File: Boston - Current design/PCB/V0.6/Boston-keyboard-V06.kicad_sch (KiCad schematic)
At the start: 601 parts, among them J701 Conn_01x02_Female, J702 Conn_01x03_Female, J705 TYPE-C-31-M12_13, J706 Conn_ARM_JTAG_SWD_10, Q701 DTC123J, Q702 AO4406AL, SW1 MXSwitch, SW10 MXSwitch, SW100 MXSwitch, SW101 MXSwitch, SW102 MXSwitch, SW103 MXSwitch, SW104 MXSwitch, SW105-1 MXSwitch, SW105-2 MXSwitch, SW106 MXSwitch, SW107 MXSwitch, SW108 MXSwitch, SW109 MXSwitch, SW11 MXSwitch, SW110 MXSwitch, SW111 MXSwitch, SW112 MXSwitch, SW113 MXSwitch, SW114 MXSwitch, SW115 MXSwitch, SW116 MXSwitch, SW117 MXSwitch, SW118 MXSwitch, SW119 MXSwitch, SW12 MXSwitch, SW120 MXSwitch, SW121 MXSwitch, SW122 MXSwitch, SW123 MXSwitch, SW124-1 MXSwitch, SW124-2 MXSwitch, SW125 MXSwitch, SW126 Rotary_Encoder_Switch_Chassis, SW127 MXSwitch, SW128 MXSwitch, SW129 MXSwitch, SW13 MXSwitch, SW14 MXSwitch, SW15 MXSwitch, SW16 MXSwitch, SW17 MXSwitch, SW18 MXSwitch, SW19 MXSwitch, SW2 MXSwitch, SW20-1 MXSwitch, SW20-2 MXSwitch, SW200 SW_Push, SW21 MXSwitch, SW22 MXSwitch, SW23 MXSwitch, SW24 MXSwitch, SW25 MXSwitch, SW26 MXSwitch, SW27 MXSwitch, SW28 MXSwitch, SW29 MXSwitch, SW3 MXSwitch, SW30 MXSwitch, SW31 MXSwitch, SW32 MXSwitch, SW33 MXSwitch, SW34 MXSwitch, SW35 MXSwitch, SW36 MXSwitch, SW37 MXSwitch, SW38 MXSwitch, SW39-1 MXSwitch, SW39-2 MXSwitch, SW39-3 MXSwitch, SW4-1 MXSwitch, SW4-2 MXSwitch, SW40 MXSwitch, SW41 MXSwitch, SW42 MXSwitch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

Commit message: Added capacitors to reduce EMI from backlight
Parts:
- added C2, C720, C723, C726, C727, C730, C731, C734, C735, C737, C738, C741, C742, C745, C746: 100nF, Capacitor_SMD:C_0805_2012Metric_Pad1.15x1.40mm_HandSolder, symbol Device:C
- added C716: 100n, Capacitor_SMD:C_0805_2012Metric_Pad1.15x1.40mm_HandSolder, symbol Device:C
- added C717, C718: 22uF, Capacitor_SMD:C_1206_3216Metric_Pad1.42x1.75mm_HandSolder, symbol Device:C
- added C721, C722, C724, C725, C728, C729, C732, C733, C736, C739, C740, C743, C744: 10u, Capacitor_SMD:C_1206_3216Metric_Pad1.42x1.75mm_HandSolder, symbol Device:C
- C704, C713: value 10u -> 22uF
- C711: value 22uF -> 10u
- L701: value L -> 6.8uH; footprint Inductor_SMD:L_Taiyo-Yuden_NR-50xx_HandSoldering -> SumidaInductor:Sumida0624CDMCC
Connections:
- net +3V3: now also C704.1, C2.1, C717.1, C718.1, C720.1, C721.1, C722.1, C723.1, C724.1, C725.1, C726.1, C727.1, C728.1, C729.1, C730.1, C731.1, C732.1, C733.1, C734.1, C735.1, C736.1, C737.1, C738.1, C739.1, C740.1, C741.1, C742.1, C743.1, C744.1, C745.1, C746.1
- net +5V: now also C716.1; no longer C704.1
- net GND: now also C716.2, C717.2, C718.2, C720.2; no longer C711.2
- net LED_switch: now also C711.2, C2.2, C721.2, C722.2, C723.2, C724.2, C725.2, C726.2, C727.2, C728.2, C729.2, C730.2, C731.2, C732.2, C733.2, C734.2, C735.2, C736.2, C737.2, C738.2, C739.2, C740.2, C741.2, C742.2, C743.2, C744.2, C745.2, C746.2
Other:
- note added: "Sumida 0624CDMCCDS-6R8MC"

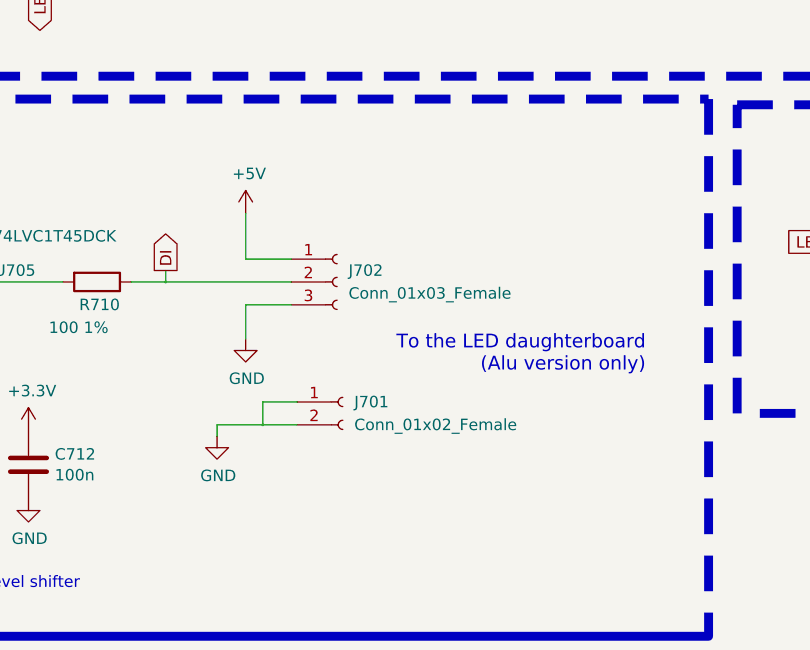
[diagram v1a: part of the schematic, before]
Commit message: More vias and tuning of ground planes for EMI purposes
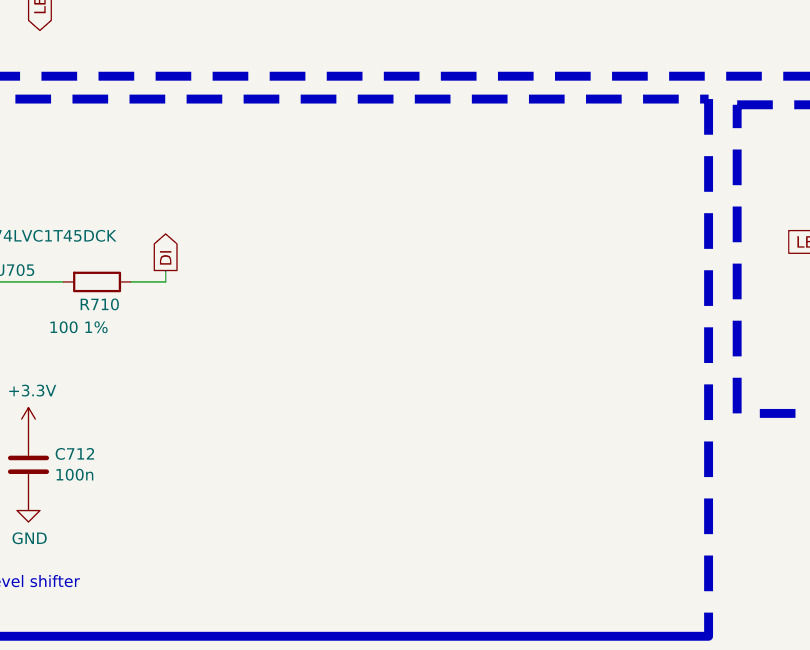
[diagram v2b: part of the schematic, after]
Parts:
- removed J701: Conn_01x02_Female, Connector_PinSocket_2.54mm:PinSocket_1x02_P2.54mm_Vertical, symbol Connector:Conn_01x02_Female
- removed J702: Conn_01x03_Female, Connector_PinSocket_2.54mm:PinSocket_1x03_P2.54mm_Vertical, symbol Connector:Conn_01x03_Female
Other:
- note removed: "To the LED daughterboard (Alu version only)"
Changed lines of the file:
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@@
   (junction (at 205.74 176.53) (diameter 0.3048) (color 0 0 0 0))
   (junction (at 205.74 204.47) (diameter 0.3048) (color 0 0 0 0))
-  (junction (at 205.74 469.265) (diameter 0.3048) (color 0 0 0 0))
   (junction (at 207.01 233.68) (diameter 0.3048) (color 0 0 0 0))
   (junction (at 208.28 234.95) (diameter 0.3048) (color 0 0 0 0))
@@
   (junction (at 213.36 408.94) (diameter 0.3048) (color 0 0 0 0))
   (junction (at 213.36 424.18) (diameter 0.3048) (color 0 0 0 0))
-  (junction (at 216.535 485.14) (diameter 0.3048) (color 0 0 0 0))
   (junction (at 217.17 35.56) (diameter 0.3048) (color 0 0 0 0))
   (junction (at 217.17 62.23) (diameter 0.3048) (color 0 0 0 0))
@@
     (stroke (width 0) (type solid) (color 0 0 0 0))
   )
-  (wire (pts (xy 205.74 469.265) (xy 219.71 469.265))
-    (stroke (width 0) (type solid) (color 0 0 0 0))
-  )
   (wire (pts (xy 207.01 233.68) (xy 205.74 233.68))
     (stroke (width 0) (type solid) (color 0 0 0 0))
@@
     (stroke (width 0) (type solid) (color 0 0 0 0))
   )
-  (wire (pts (xy 211.455 485.14) (xy 216.535 485.14))
-    (stroke (width 0) (type solid) (color 0 0 0 0))
-  )
-  (wire (pts (xy 211.455 486.41) (xy 211.455 485.14))
-    (stroke (width 0) (type solid) (color 0 0 0 0))
-  )
   (wire (pts (xy 213.36 283.21) (xy 204.47 283.21))
     (stroke (width 0) (type solid) (color 0 0 0 0))
@@
     (stroke (width 0) (type solid) (color 0 0 0 0))
   )
-  (wire (pts (xy 214.63 466.725) (xy 214.63 461.645))
-    (stroke (width 0) (type solid) (color 0 0 0 0))
-  )
-  (wire (pts (xy 214.63 471.805) (xy 214.63 475.615))
-    (stroke (width 0) (type solid) (color 0 0 0 0))
-  )
-  (wire (pts (xy 216.535 482.6) (xy 216.535 485.14))
-    (stroke (width 0) (type solid) (color 0 0 0 0))
-  )
-  (wire (pts (xy 216.535 485.14) (xy 220.345 485.14))
-    (stroke (width 0) (type solid) (color 0 0 0 0))
-  )
   (wire (pts (xy 217.17 35.56) (xy 182.88 35.56))
     (stroke (width 0) (type solid) (color 0 0 0 0))
@@
     (stroke (width 0) (type solid) (color 0 0 0 0))
   )
-  (wire (pts (xy 219.71 466.725) (xy 214.63 466.725))
-    (stroke (width 0) (type solid) (color 0 0 0 0))
-  )
-  (wire (pts (xy 219.71 471.805) (xy 214.63 471.805))
-    (stroke (width 0) (type solid) (color 0 0 0 0))
-  )
-  (wire (pts (xy 220.345 482.6) (xy 216.535 482.6))
-    (stroke (width 0) (type solid) (color 0 0 0 0))
-  )
   (wire (pts (xy 222.25 283.21) (xy 213.36 283.21))
     (stroke (width 0) (type solid) (color 0 0 0 0))
@@
     (effects (font (size 1.27 1.27)) (justify left bottom))
   )
-  (text "To the LED daughterboard\n(Alu version only)" (at 259.08 479.425 180)
-    (effects (font (size 1.524 1.524)) (justify right bottom))
-  )
   (text "RGB LED stuff" (at 266.7 514.985 180)
     (effects (font (size 3.175 3.175)) (justify right bottom))
@@
     (pin "1")
   )
-  (symbol (lib_id "power:+5V") (at 214.63 461.645 0) (unit 1)
-    (in_bom yes) (on_board yes)
-    (property "Reference" "#PWR0108" (id 0) (at 214.63 465.455 0)
-      (effects (font (size 1.27 1.27)) hide)
-    )
-    (property "Value" "+5V" (id 1) (at 215.011 457.2508 0))
-    (property "Footprint" "" (id 2) (at 214.63 461.645 0)
-      (effects (font (size 1.27 1.27)) hide)
-    )
-    (property "Datasheet" "" (id 3) (at 214.63 461.645 0)
-      (effects (font (size 1.27 1.27)) hide)
-    )
-    (pin "1")
-  )
   (symbol (lib_id "power:+3.3V") (at 315.595 389.255 0) (unit 1)
     (in_bom yes) (on_board yes)
@@
     (pin "1")
   )
-  (symbol (lib_id "power:GND") (at 211.455 486.41 0) (unit 1)
-    (in_bom yes) (on_board yes)
-    (property "Reference" "#PWR0701" (id 0) (at 211.455 492.76 0)
-      (effects (font (size 1.27 1.27)) hide)
-    )
-    (property "Value" "GND" (id 1) (at 211.582 490.8042 0))
-    (property "Footprint" "" (id 2) (at 211.455 486.41 0)
-      (effects (font (size 1.27 1.27)) hide)
-    )
-    (property "Datasheet" "" (id 3) (at 211.455 486.41 0)
-      (effects (font (size 1.27 1.27)) hide)
-    )
-    (pin "1")
-  )
-  (symbol (lib_id "power:GND") (at 214.63 475.615 0) (unit 1)
-    (in_bom yes) (on_board yes)
-    (property "Reference" "#PWR0109" (id 0) (at 214.63 481.965 0)
-      (effects (font (size 1.27 1.27)) hide)
-    )
-    (property "Value" "GND" (id 1) (at 214.757 480.0092 0))
-    (property "Footprint" "" (id 2) (at 214.63 475.615 0)
-      (effects (font (size 1.27 1.27)) hide)
-    )
-    (property "Datasheet" "" (id 3) (at 214.63 475.615 0)
-      (effects (font (size 1.27 1.27)) hide)
-    )
-    (pin "1")
-  )
   (symbol (lib_id "power:GND") (at 314.96 476.25 0) (unit 1)
     (in_bom yes) (on_board yes)
@@
     (pin "2")
   )
-  (symbol (lib_id "Connector:Conn_01x02_Female") (at 225.425 482.6 0) (unit 1)
-    (in_bom yes) (on_board yes)
-    (property "Reference" "J701" (id 0) (at 226.695 482.6 0)
-      (effects (font (size 1.27 1.27)) (justify left))
-    )
-    (property "Value" "Conn_01x02_Female" (id 1) (at 226.695 485.14 0)
-      (effects (font (size 1.27 1.27)) (justify left))
-    )
-    (property "Footprint" "Connector_PinSocket_2.54mm:PinSocket_1x02_P2.54mm_Vertical" (id 2) (at 225.425 482.6 0)
-      (effects (font (size 1.27 1.27)) hide)
-    )
-    (property "Datasheet" "~" (id 3) (at 225.425 482.6 0)
-      (effects (font (size 1.27 1.27)) hide)
-    )
-    (pin "1")
-    (pin "2")
-  )
   (symbol (lib_id "Device:LED") (at 19.05 337.82 90) (unit 1)
     (in_bom yes) (on_board yes)
@@
     (pin "2")
   )
-  (symbol (lib_id "Connector:Conn_01x03_Female") (at 224.79 469.265 0) (unit 1)
-    (in_bom yes) (on_board yes)
-    (property "Reference" "J702" (id 0) (at 226.06 467.995 0)
-      (effects (font (size 1.27 1.27)) (justify left))
-    )
-    (property "Value" "Conn_01x03_Female" (id 1) (at 226.06 470.535 0)
-      (effects (font (size 1.27 1.27)) (justify left))
-    )
-    (property "Footprint" "Connector_PinSocket_2.54mm:PinSocket_1x03_P2.54mm_Vertical" (id 2) (at 224.79 469.265 0)
-      (effects (font (size 1.27 1.27)) hide)
-    )
-    (property "Datasheet" "~" (id 3) (at 224.79 469.265 0)
-      (effects (font (size 1.27 1.27)) hide)
-    )
-    (pin "1")
-    (pin "2")
-    (pin "3")
-  )
   (symbol (lib_id "Boston-controller-STM32-rescue:AO4406AL-Acheron") (at 314.96 464.82 0) (unit 1)
     (in_bom yes) (on_board yes)
@@
       (reference "#PWR0107") (unit 1) (value "GND") (footprint "")
     )
-    (path "/3768f2ad-ca0d-45b9-a5b6-acf6323cf77c"
-      (reference "#PWR0108") (unit 1) (value "+5V") (footprint "")
-    )
-    (path "/8e4114e4-bab9-46e1-94cf-1b7870f26a9b"
-      (reference "#PWR0109") (unit 1) (value "GND") (footprint "")
-    )
     (path "/e0d0e651-212d-4330-89d4-7486aed51f96"
       (reference "#PWR0110") (unit 1) (value "GND") (footprint "")
@@
       (reference "#PWR0131") (unit 1) (value "+5V") (footprint "")
     )
-    (path "/16a48369-f521-4059-84e3-285af70b1624"
-      (reference "#PWR0701") (unit 1) (value "GND") (footprint "")
-    )
     (path "/138f3822-fcf4-4fa8-92fd-af4a95c5f1d7"
       (reference "#PWR0702") (unit 1) (value "+5V") (footprint "")
@@
       (reference "HA4") (unit 1) (value "MountingHole") (footprint "acheronMountingHoles:ToolingHole_1.152mm_(for_JLCPCB_SMT)")
     )
-    (path "/7ed23066-3dd3-44f1-8df7-891da9ec2408"
-      (reference "J701") (unit 1) (value "Conn_01x02_Female") (footprint "Connector_PinSocket_2.54mm:PinSocket_1x02_P2.54mm_Vertical")
-    )
-    (path "/44a6e241-6dc6-4665-9e45-58d103d8eab1"
-      (reference "J702") (unit 1) (value "Conn_01x03_Female") (footprint "Connector_PinSocket_2.54mm:PinSocket_1x03_P2.54mm_Vertical")
-    )
     (path "/00000000-0000-0000-0000-00005dd1170a"
